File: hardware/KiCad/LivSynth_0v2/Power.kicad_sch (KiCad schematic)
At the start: 61 parts, among them J12 VGND, J201 Test Points, J24 3V3, J25 9V, J7 Barrel_Jack_Switch, Q3 AO3401A, SW7 SW_SPDT, U1 TL074, U12 TPS63070, U2 TL074, U4 TL074, U5 TL074, U6 TL074, U7 LM13700, U8 LM1117-3.3

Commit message: Create new 0v3 folder
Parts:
- R96: LCSC C25803 -> (none)
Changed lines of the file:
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@@
-      (effects (font (size 1.27 1.27)) hide)
-    )
-    (property "LCSC" "C25803" (id 4) (at 139.065 88.9 0)
       (effects (font (size 1.27 1.27)) hide)
     )

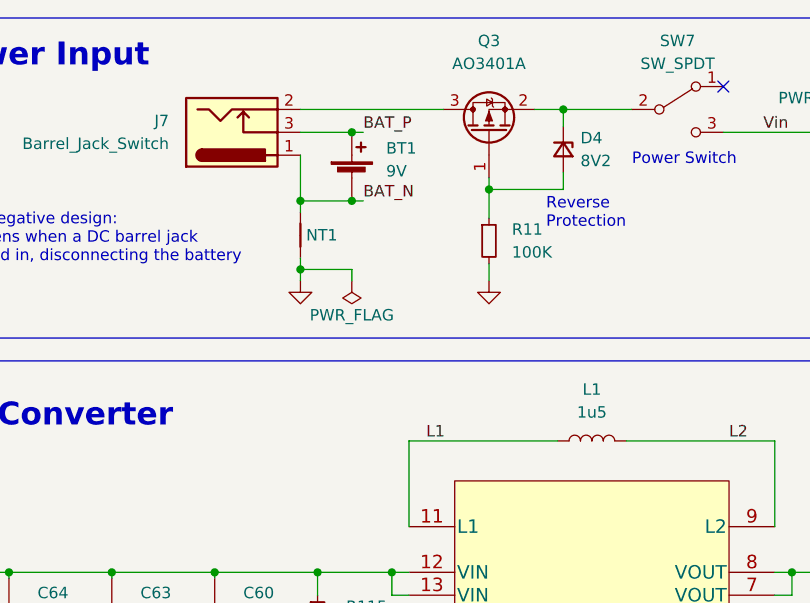
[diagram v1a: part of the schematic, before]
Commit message: Reduce EG cap to 4u7 Reduce LFO cap to 220n VCO R23: 470K, C13: 10n
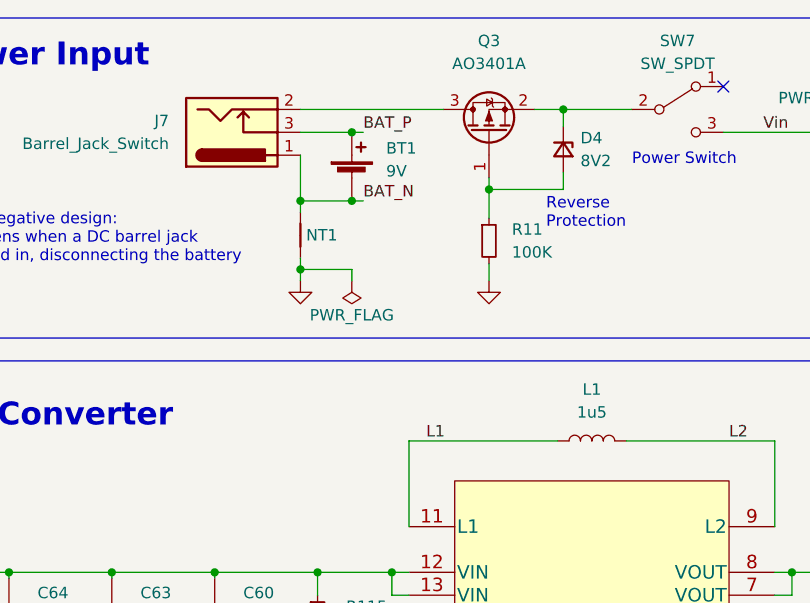
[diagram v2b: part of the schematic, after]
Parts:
- R96: LCSC (none) -> C25803
